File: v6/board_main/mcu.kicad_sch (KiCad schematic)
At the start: 39 parts, among them J2 Micro_SD_Card, J3 Pico Debugger (SWD), U10 W25Q16JVUXIQ, U11 RP2350A, U8 Pi-Radio, Y1 KX7_QRZ

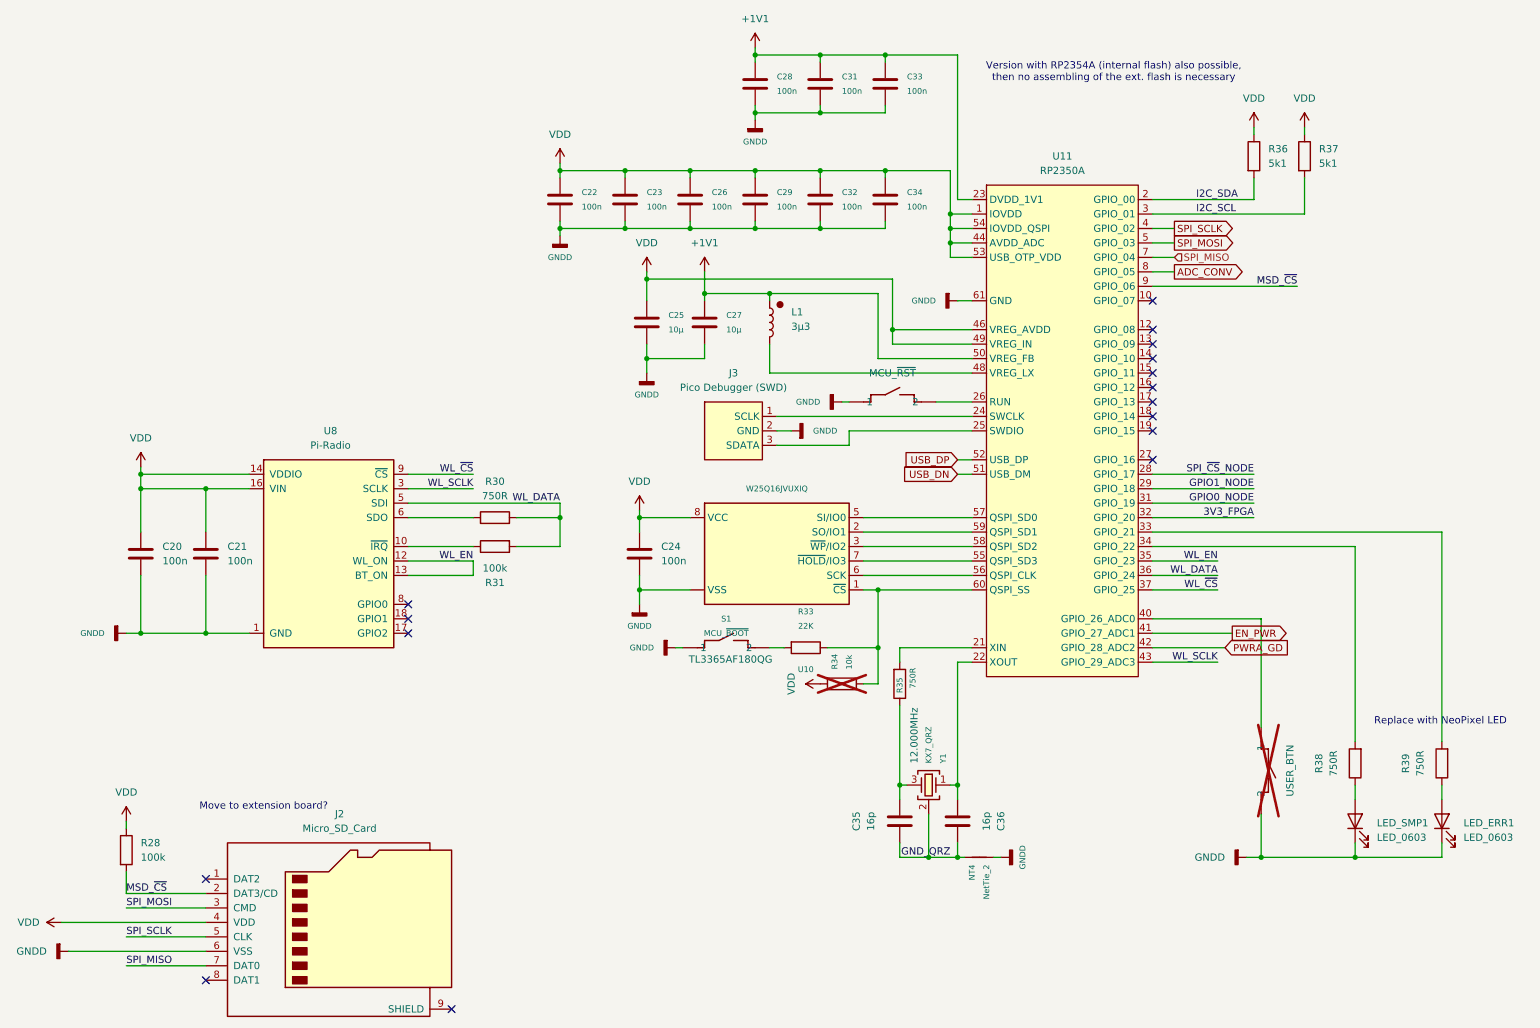
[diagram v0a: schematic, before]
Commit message: Rephrasing ENV5 design
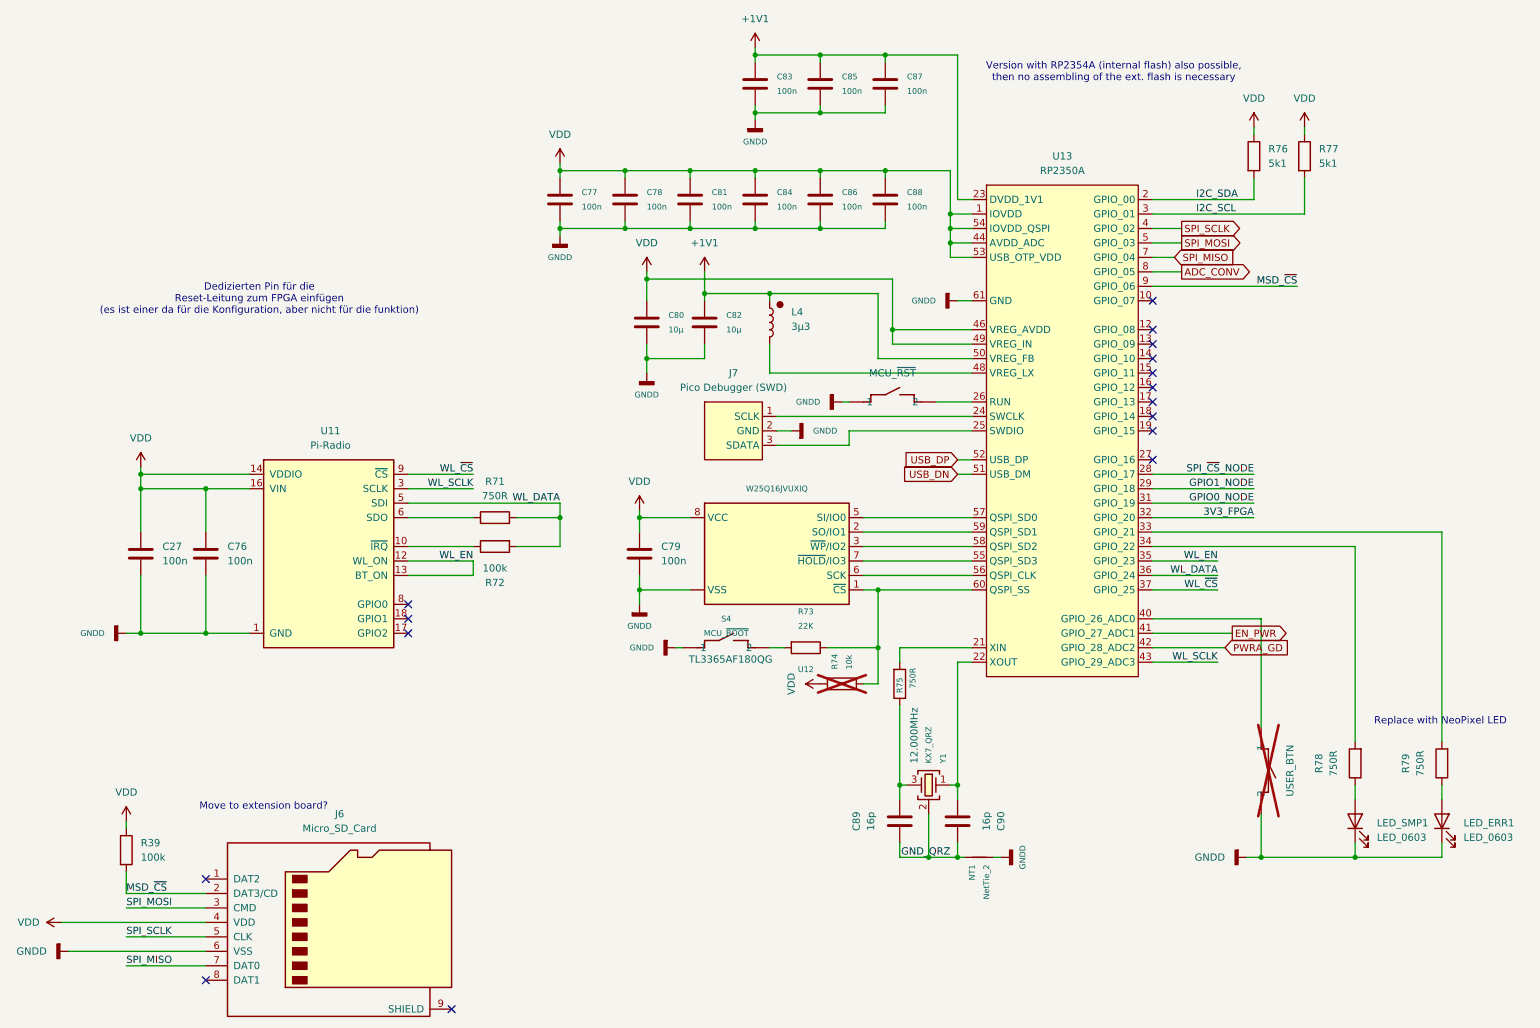
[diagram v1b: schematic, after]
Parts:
- renumbered C20 to C27, C21 to C76, C22 to C77, C23 to C78, C24 to C79, C25 to C80, C26 to C81, C27 to C82, C28 to C83, C29 to C84, C31 to C85, C32 to C86, C33 to C87, C34 to C88, C35 to C89, C36 to C90, J2 to J6, J3 to J7, L1 to L4, NT4 to NT1, R28 to R39, R30 to R71, R31 to R72, R33 to R73, R34 to R74, R35 to R75, R36 to R76, R37 to R77, R38 to R78, R39 to R79, S1 to S4, S2 to S5, S3 to S6, U8 to U11, U10 to U12, U11 to U13
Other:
- note added: "Dedizierten Pin für die Reset-Leitung zum FPGA einfügen (es ist einer da für die Konfiguration, aber nicht für die funktion)"
